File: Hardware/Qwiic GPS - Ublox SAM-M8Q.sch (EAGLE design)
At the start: 32 parts, among them J3 PTH, U2 SAM-M8Q

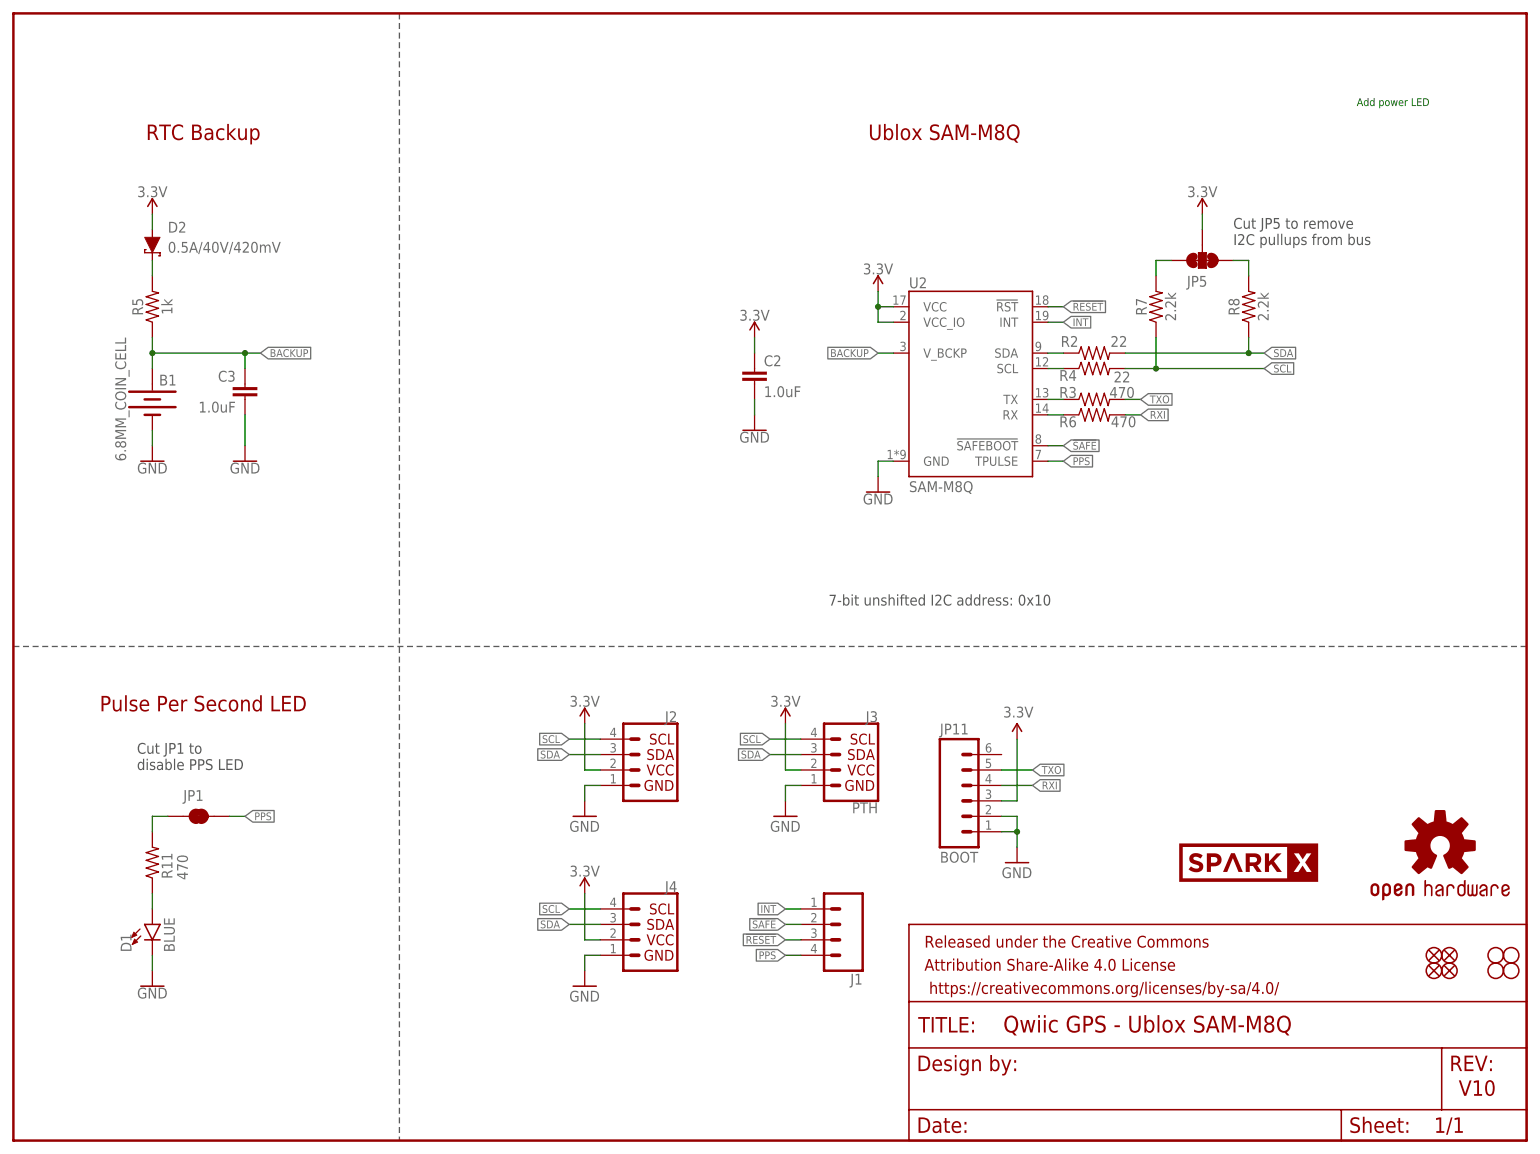
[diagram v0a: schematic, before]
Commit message: Removing single unit files. Removing notes from schematic.
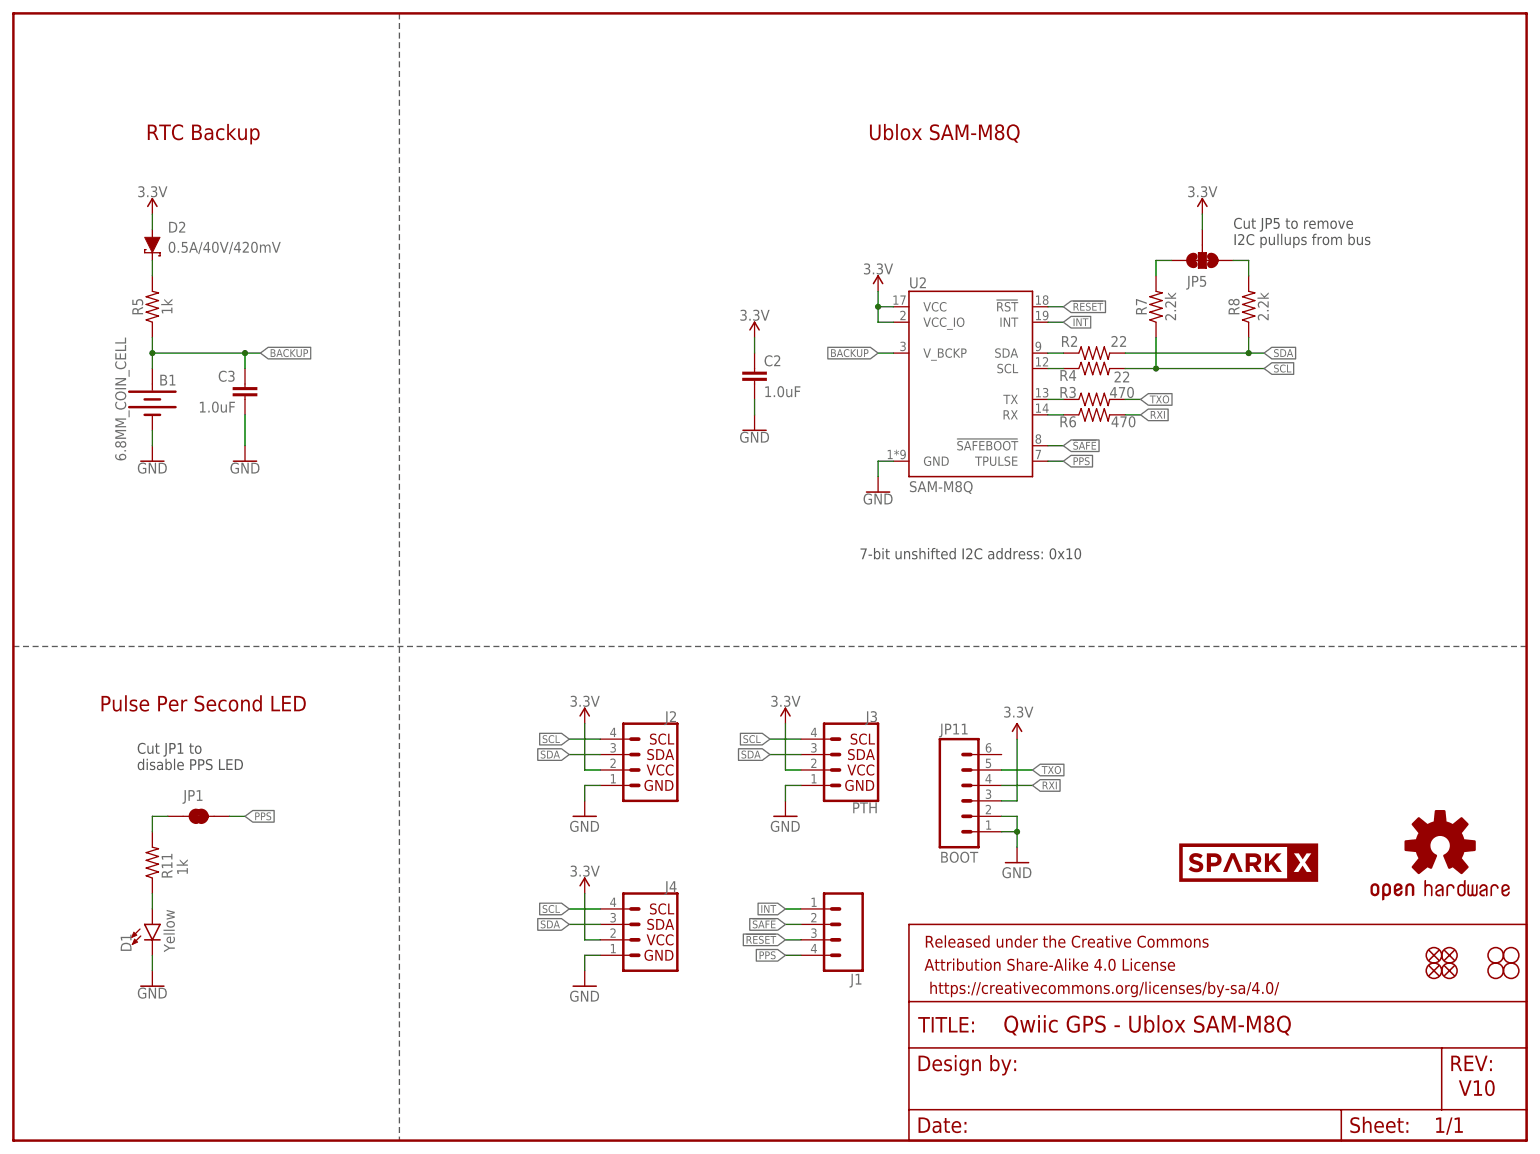
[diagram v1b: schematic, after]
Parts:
- D1: value BLUE -> Yellow; device SparkFun-LED:LED-BLUE0603 -> SparkFun-LED:LED-YELLOW0603
- R11: value 470 -> 1k; device SparkFun-Resistors:470OHM-0603-1/10W-1% -> SparkFun-Resistors:1KOHM-0603-1/10W-1%
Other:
- note removed: "Add power LED"

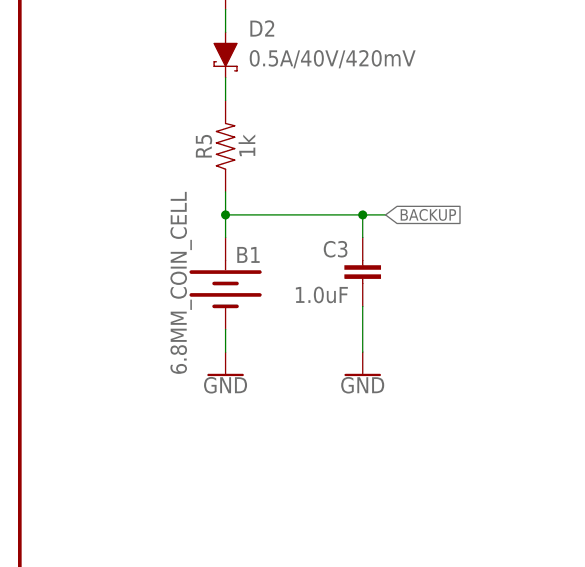
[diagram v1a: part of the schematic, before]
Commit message: Updated battery footprint
Footprint for the battery is now for the reflowable version
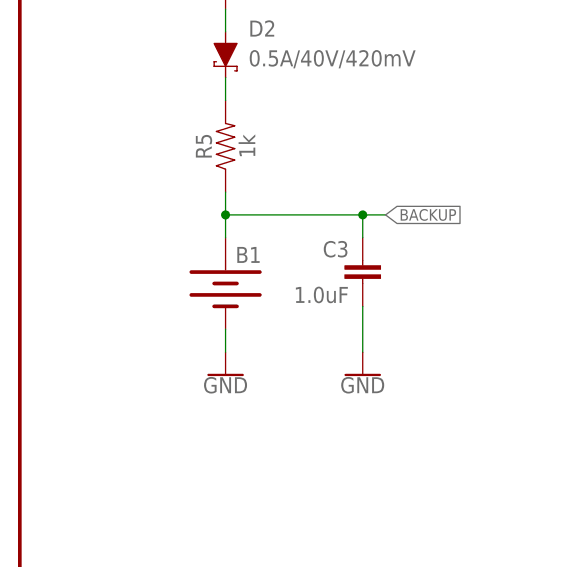
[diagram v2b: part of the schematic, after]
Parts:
- B1: device SparkFun-Batteries:BATTERY-6.8MM_SMD -> SparkFun-Batteries:ML414H_IV01E_BATTERY
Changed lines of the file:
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@@
 <?xml version="1.0" encoding="utf-8"?>
 <!DOCTYPE eagle SYSTEM "eagle.dtd">
-<eagle version="9.2.1">
+<eagle version="9.3.0">
 <drawing>
 <settings>
@@
 <part name="R6" library="SparkFun-Resistors" deviceset="470OHM" device="-0603-1/10W-1%" value="470"/>
 <part name="C3" library="SparkFun-Capacitors" deviceset="1.0UF" device="-0603-16V-10%" value="1.0uF"/>
-<part name="B1" library="SparkFun-Batteries" deviceset="BATTERY" device="-6.8MM_SMD" value="6.8MM_COIN_CELL"/>
+<part name="B1" library="SparkFun-Batteries" deviceset="ML414H_IV01E_BATTERY" device="" value="6.8MM_COIN_CELL"/>
 <part name="GND5" library="SparkFun-PowerSymbols" deviceset="GND" device=""/>
 <part name="GND10" library="SparkFun-PowerSymbols" deviceset="GND" device=""/>
@@
 <instance part="B1" gate="G$1" x="22.86" y="121.92" smashed="yes" rot="R270">
 <attribute name="NAME" x="25.4" y="124.206" size="1.778" layer="95" font="vector" rot="MR0" align="bottom-center"/>
-<attribute name="VALUE" x="18.542" y="121.92" size="1.778" layer="96" font="vector" rot="R270" align="top-center"/>
 </instance>
 <instance part="GND5" gate="1" x="22.86" y="111.76" smashed="yes">
